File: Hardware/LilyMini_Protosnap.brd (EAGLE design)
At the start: 77.5 x 53.3 mm, 77 parts, among them Q1 ZXMP6A13F, U1 SAMD11D14A-M, U2 AP2112K-3.3V, U3 ALS-PT19, Y1 32.768kHz

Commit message: Minor tweaks per board review checklist
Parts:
- LOGO4: value (none) -> SFE_LOGO_NAME.1_INCH
- renumbered U$3 to LOGO4
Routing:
- net !RST!: track 26.5 -> 28.9 mm
- net !RST!1: track 18.7 -> 20.0 mm
- net GND: vias 12 -> 11
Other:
- board text added: "NOTE 31 MIL / 0.8MM BOARD THICKNESS"
- board text added: "ROUTE OUT"
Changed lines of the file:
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@@
 <layer number="14" name="Route14" color="1" fill="6" visible="no" active="no"/>
 <layer number="15" name="Route15" color="4" fill="6" visible="no" active="no"/>
-<layer number="16" name="Bottom" color="1" fill="1" visible="yes" active="yes"/>
-<layer number="17" name="Pads" color="2" fill="1" visible="yes" active="yes"/>
-<layer number="18" name="Vias" color="2" fill="1" visible="yes" active="yes"/>
-<layer number="19" name="Unrouted" color="6" fill="1" visible="yes" active="yes"/>
+<layer number="16" name="Bottom" color="1" fill="1" visible="no" active="yes"/>
+<layer number="17" name="Pads" color="2" fill="1" visible="no" active="yes"/>
+<layer number="18" name="Vias" color="2" fill="1" visible="no" active="yes"/>
+<layer number="19" name="Unrouted" color="6" fill="1" visible="no" active="yes"/>
 <layer number="20" name="Dimension" color="15" fill="1" visible="yes" active="yes"/>
 <layer number="21" name="tPlace" color="7" fill="1" visible="no" active="yes"/>
-<layer number="22" name="bPlace" color="7" fill="1" visible="yes" active="yes"/>
+<layer number="22" name="bPlace" color="7" fill="1" visible="no" active="yes"/>
 <layer number="23" name="tOrigins" color="15" fill="1" visible="no" active="yes"/>
-<layer number="24" name="bOrigins" color="15" fill="1" visible="yes" active="yes"/>
+<layer number="24" name="bOrigins" color="15" fill="1" visible="no" active="yes"/>
 <layer number="25" name="tNames" color="7" fill="1" visible="no" active="yes"/>
 <layer number="26" name="bNames" color="7" fill="1" visible="no" active="yes"/>
@@
 <layer number="28" name="bValues" color="7" fill="1" visible="no" active="yes"/>
 <layer number="29" name="tStop" color="7" fill="3" visible="no" active="yes"/>
-<layer number="30" name="bStop" color="7" fill="6" visible="yes" active="yes"/>
+<layer number="30" name="bStop" color="7" fill="6" visible="no" active="yes"/>
 <layer number="31" name="tCream" color="7" fill="4" visible="no" active="yes"/>
 <layer number="32" name="bCream" color="7" fill="5" visible="no" active="yes"/>
@@
 <layer number="37" name="tTest" color="7" fill="1" visible="no" active="yes"/>
 <layer number="38" name="bTest" color="7" fill="1" visible="no" active="yes"/>
-<layer number="39" name="tKeepout" color="4" fill="11" visible="yes" active="yes"/>
+<layer number="39" name="tKeepout" color="4" fill="11" visible="no" active="yes"/>
 <layer number="40" name="bKeepout" color="1" fill="11" visible="no" active="yes"/>
-<layer number="41" name="tRestrict" color="4" fill="10" visible="yes" active="yes"/>
+<layer number="41" name="tRestrict" color="4" fill="10" visible="no" active="yes"/>
 <layer number="42" name="bRestrict" color="1" fill="10" visible="no" active="yes"/>
 <layer number="43" name="vRestrict" color="2" fill="10" visible="no" active="yes"/>
@@
 <layer number="45" name="Holes" color="7" fill="1" visible="no" active="yes"/>
 <layer number="46" name="Milling" color="3" fill="1" visible="no" active="yes"/>
-<layer number="47" name="Measures" color="7" fill="1" visible="yes" active="yes"/>
+<layer number="47" name="Measures" color="7" fill="1" visible="no" active="yes"/>
 <layer number="48" name="Document" color="7" fill="1" visible="no" active="yes"/>
 <layer number="49" name="Reference" color="7" fill="1" visible="no" active="yes"/>
@@
 G 6
 B 7</text>
+<text x="38.735" y="-7.62" size="1.778" layer="51" align="center">NOTE 31 MIL / 0.8MM BOARD THICKNESS</text>
+<text x="39.52875" y="7.14375" size="0.6096" layer="20" ratio="10" align="center">ROUTE OUT</text>
+<text x="39.21125" y="43.65625" size="0.6096" layer="20" ratio="10" align="center">ROUTE OUT</text>
+<text x="67.78625" y="39.21125" size="0.6096" layer="20" ratio="10" align="center">ROUTE OUT</text>
+<text x="67.945" y="33.17875" size="0.6096" layer="20" ratio="10" align="center">ROUTE OUT</text>
+<text x="67.945" y="30.95625" size="0.6096" layer="20" ratio="10" align="center">ROUTE OUT</text>
+<text x="67.945" y="24.92375" size="0.6096" layer="20" ratio="10" align="center">ROUTE OUT</text>
+<text x="67.945" y="20.16125" size="0.6096" layer="20" ratio="10" align="center">ROUTE OUT</text>
+<text x="67.945" y="14.12875" size="0.6096" layer="20" ratio="10" align="center">ROUTE OUT</text>
+<text x="67.945" y="5.87375" size="0.6096" layer="20" ratio="10" align="center">ROUTE OUT</text>
+<text x="12.065" y="7.14375" size="0.6096" layer="20" ratio="10" align="center">ROUTE OUT</text>
+<text x="12.065" y="15.71625" size="0.6096" layer="20" ratio="10" align="center">ROUTE OUT</text>
+<text x="12.7" y="50.8" size="0.6096" layer="20" ratio="10" align="center">ROUTE OUT</text>
+<text x="23.495" y="34.29" size="0.6096" layer="20" ratio="10" rot="R60" align="center">ROUTE OUT</text>
+<text x="55.245" y="16.35125" size="0.6096" layer="20" ratio="10" rot="R60" align="center">ROUTE OUT</text>
+<text x="55.245" y="34.29" size="0.6096" layer="20" ratio="10" rot="R120" align="center">ROUTE OUT</text>
+<text x="23.65375" y="16.1925" size="0.6096" layer="20" ratio="10" rot="R120" align="center">ROUTE OUT</text>
+<text x="3.96875" y="35.40125" size="0.6096" layer="20" ratio="10" rot="R120" align="center">ROUTE OUT</text>
+<text x="21.59" y="35.71875" size="0.6096" layer="20" ratio="10" rot="R60" align="center">ROUTE OUT</text>
 </plain>
 <attributes>
@@
 <element name="JP24" library="LilyPad-Wearables" package="PETAL-SMALL-2SIDE" value="" x="63.5" y="36.195" rot="R270"/>
 <element name="JP26" library="LilyPad-Wearables" package="PETAL-SMALL-2SIDE" value="" x="63.5" y="27.94" rot="R270"/>
-<element name="U$3" library="SparkFun-Aesthetics" package="SFE_LOGO_NAME_.1" value="" x="45.72" y="44.92625" rot="MR0"/>
 <element name="U$4" library="SparkFun-Aesthetics" package="SFE_LOGO_FLAME_COPPER_EXPOSED_.1" value="" x="39.21125" y="47.625" rot="MR0"/>
 <element name="FD2" library="SparkFun-Aesthetics" package="MICRO-FIDUCIAL" value="FIDUCIALUFIDUCIAL" x="73.66" y="3.81"/>
@@
 <element name="FD3" library="SparkFun-Aesthetics" package="MICRO-FIDUCIAL" value="FIDUCIALUFIDUCIAL" x="3.81" y="49.53" rot="MR0"/>
 <element name="FD4" library="SparkFun-Aesthetics" package="MICRO-FIDUCIAL" value="FIDUCIALUFIDUCIAL" x="73.66" y="3.81" rot="MR0"/>
+<element name="LOGO4" library="SparkFun-Aesthetics" package="SFE_LOGO_NAME_.1" value="SFE_LOGO_NAME.1_INCH" x="45.72" y="44.92625" rot="MR0"/>
 </elements>
 <signals>
@@
 <contactref element="JP9" pad="P$1"/>
 <wire x1="30.7975" y1="23.1775" x2="38.1" y2="15.875" width="0.3048" layer="1"/>
-<wire x1="43.815" y1="15.875" x2="45.72" y2="15.875" width="0.3048" layer="16"/>
-<wire x1="45.72" y1="15.875" x2="47.205" y2="17.36" width="0.3048" layer="16"/>
+<wire x1="43.815" y1="15.875" x2="46.99" y2="15.875" width="0.3048" layer="16"/>
+<wire x1="46.99" y1="15.875" x2="48.475" y2="17.36" width="0.3048" layer="16"/>
 <contactref element="R5" pad="2"/>
-<wire x1="47.205" y1="17.36" x2="47.205" y2="18.415" width="0.3048" layer="16"/>
+<wire x1="48.475" y1="17.36" x2="48.475" y2="18.2" width="0.3048" layer="16"/>
+<wire x1="48.475" y1="18.2" x2="48.26" y2="18.415" width="0.3048" layer="16"/>
+<wire x1="48.26" y1="18.415" x2="47.205" y2="18.415" width="0.3048" layer="16"/>
 </signal>
 <signal name="USB5V">
@@
 <via x="45.085" y="17.145" extent="1-16" drill="0.508"/>
 <via x="51.435" y="21.59" extent="1-16" drill="0.508"/>
-<via x="48.26" y="15.875" extent="1-16" drill="0.508"/>
 <contactref element="S2" pad="4"/>
 <contactref element="S2" pad="3"/>
@@
 <wire x1="35.2425" y1="23.1775" x2="38.735" y2="19.685" width="0.3048" layer="1"/>
 <wire x1="38.735" y1="19.685" x2="43.815" y2="19.685" width="0.3048" layer="1"/>
-<wire x1="45.505" y1="18.415" x2="45.505" y2="19.685" width="0.3048" layer="16"/>
 <wire x1="45.505" y1="19.685" x2="43.815" y2="19.685" width="0.3048" layer="16"/>
 <via x="43.815" y="19.685" extent="1-16" drill="0.508"/>
+<wire x1="45.505" y1="18.415" x2="44.45" y2="18.415" width="0.3048" layer="16"/>
+<wire x1="44.45" y1="18.415" x2="43.815" y2="19.05" width="0.3048" layer="16"/>
+<wire x1="43.815" y1="19.05" x2="43.815" y2="19.685" width="0.3048" layer="16"/>
 </signal>
 <signal name="X2">

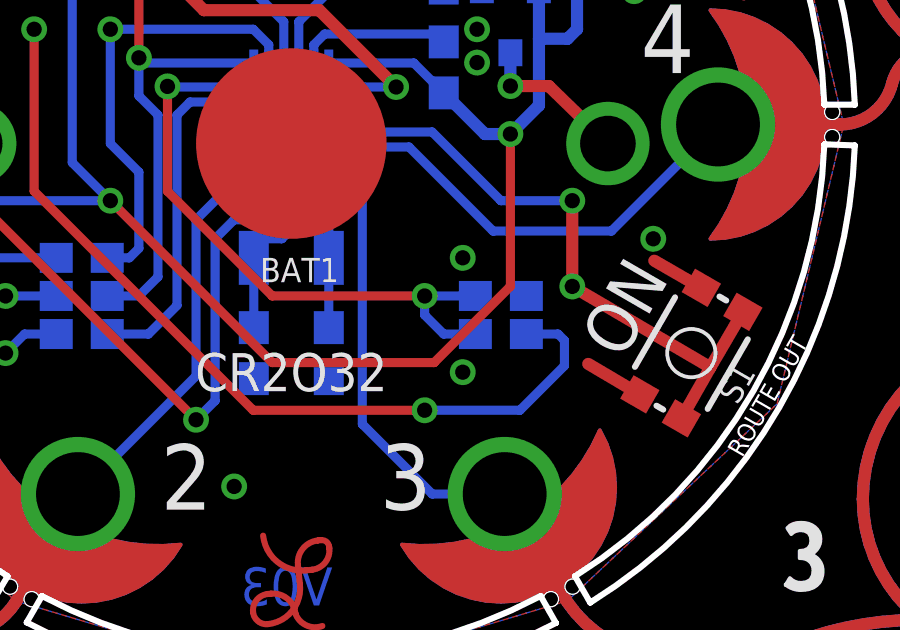
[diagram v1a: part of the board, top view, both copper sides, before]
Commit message: Minor changes based on AC and Bob's advice
Reduced paste on QFN and USB footprints by 25%
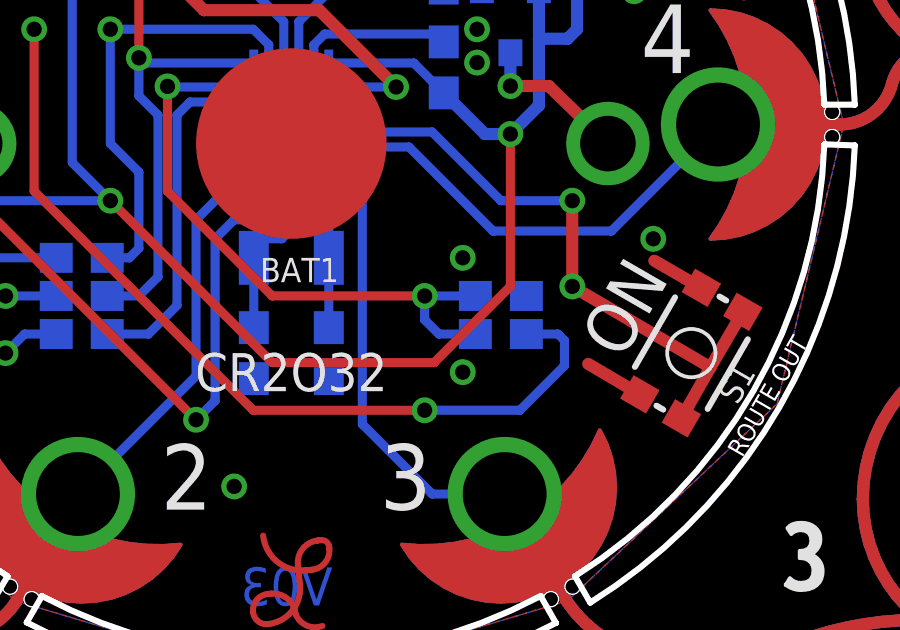
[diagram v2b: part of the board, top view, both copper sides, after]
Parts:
- JP1: value (none) -> USB_MICROB_PLUGUSB-B-MICRO-SMD-VERT
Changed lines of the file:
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@@
 <grid distance="0.025" unitdist="inch" unit="inch" style="lines" multiple="4" display="yes" altdistance="0.00625" altunitdist="inch" altunit="inch"/>
 <layers>
-<layer number="1" name="Top" color="4" fill="1" visible="no" active="yes"/>
+<layer number="1" name="Top" color="4" fill="1" visible="yes" active="yes"/>
 <layer number="2" name="Route2" color="1" fill="3" visible="no" active="no"/>
 <layer number="3" name="Route3" color="4" fill="3" visible="no" active="no"/>
@@
 <layer number="15" name="Route15" color="4" fill="6" visible="no" active="no"/>
 <layer number="16" name="Bottom" color="1" fill="1" visible="no" active="yes"/>
-<layer number="17" name="Pads" color="2" fill="1" visible="no" active="yes"/>
-<layer number="18" name="Vias" color="2" fill="1" visible="no" active="yes"/>
+<layer number="17" name="Pads" color="2" fill="1" visible="yes" active="yes"/>
+<layer number="18" name="Vias" color="2" fill="1" visible="yes" active="yes"/>
 <layer number="19" name="Unrouted" color="6" fill="1" visible="no" active="yes"/>
 <layer number="20" name="Dimension" color="15" fill="1" visible="yes" active="yes"/>
-<layer number="21" name="tPlace" color="7" fill="1" visible="no" active="yes"/>
+<layer number="21" name="tPlace" color="7" fill="1" visible="yes" active="yes"/>
 <layer number="22" name="bPlace" color="7" fill="1" visible="no" active="yes"/>
 <layer number="23" name="tOrigins" color="15" fill="1" visible="no" active="yes"/>
@@
 <layer number="27" name="tValues" color="7" fill="1" visible="no" active="yes"/>
 <layer number="28" name="bValues" color="7" fill="1" visible="no" active="yes"/>
-<layer number="29" name="tStop" color="7" fill="3" visible="no" active="yes"/>
+<layer number="29" name="tStop" color="7" fill="3" visible="yes" active="yes"/>
 <layer number="30" name="bStop" color="7" fill="6" visible="no" active="yes"/>
-<layer number="31" name="tCream" color="7" fill="4" visible="no" active="yes"/>
+<layer number="31" name="tCream" color="7" fill="4" visible="yes" active="yes"/>
 <layer number="32" name="bCream" color="7" fill="5" visible="no" active="yes"/>
 <layer number="33" name="tFinish" color="6" fill="3" visible="no" active="yes"/>
@@
 <layer number="37" name="tTest" color="7" fill="1" visible="no" active="yes"/>
 <layer number="38" name="bTest" color="7" fill="1" visible="no" active="yes"/>
-<layer number="39" name="tKeepout" color="4" fill="11" visible="no" active="yes"/>
+<layer number="39" name="tKeepout" color="4" fill="11" visible="yes" active="yes"/>
 <layer number="40" name="bKeepout" color="1" fill="11" visible="no" active="yes"/>
-<layer number="41" name="tRestrict" color="4" fill="10" visible="no" active="yes"/>
+<layer number="41" name="tRestrict" color="4" fill="10" visible="yes" active="yes"/>
 <layer number="42" name="bRestrict" color="1" fill="10" visible="no" active="yes"/>
 <layer number="43" name="vRestrict" color="2" fill="10" visible="no" active="yes"/>
@@
 <layer number="45" name="Holes" color="7" fill="1" visible="no" active="yes"/>
 <layer number="46" name="Milling" color="3" fill="1" visible="no" active="yes"/>
-<layer number="47" name="Measures" color="7" fill="1" visible="no" active="yes"/>
+<layer number="47" name="Measures" color="7" fill="1" visible="yes" active="yes"/>
 <layer number="48" name="Document" color="7" fill="1" visible="no" active="yes"/>
 <layer number="49" name="Reference" color="7" fill="1" visible="no" active="yes"/>
 <layer number="50" name="dxf" color="7" fill="1" visible="no" active="no"/>
-<layer number="51" name="tDocu" color="7" fill="1" visible="no" active="yes"/>
+<layer number="51" name="tDocu" color="7" fill="1" visible="yes" active="yes"/>
 <layer number="52" name="bDocu" color="7" fill="1" visible="no" active="yes"/>
 <layer number="53" name="tGND_GNDA" color="7" fill="9" visible="no" active="no"/>
@@
 <elements>
 <element name="FRAME1" library="SparkFun-Aesthetics" package="CREATIVE_COMMONS" value="FRAME-LETTER" x="4.445" y="-17.78"/>
-<element name="JP1" library="mike-temp" package="USB-B-MICRO-SMD_VERT" value="" x="39.37" y="38.4175" smashed="yes">
+<element name="JP1" library="mike-temp" package="USB-B-MICRO-SMD_VERT" value="USB_MICROB_PLUGUSB-B-MICRO-SMD-VERT" x="39.37" y="38.4175" smashed="yes">
 <attribute name="NAME" x="40.275" y="40.4975" size="0.8128" layer="25" align="bottom-right"/>
 <attribute name="VALUE" x="40.37" y="35.4175" size="0.4064" layer="27"/>
@@
 <wire x1="45.505" y1="19.685" x2="43.815" y2="19.685" width="0.3048" layer="16"/>
 <via x="43.815" y="19.685" extent="1-16" drill="0.508"/>
-<wire x1="45.505" y1="18.415" x2="44.45" y2="18.415" width="0.3048" layer="16"/>
-<wire x1="44.45" y1="18.415" x2="43.815" y2="19.05" width="0.3048" layer="16"/>
-<wire x1="43.815" y1="19.05" x2="43.815" y2="19.685" width="0.3048" layer="16"/>
+<wire x1="45.505" y1="18.415" x2="44.29125" y2="18.415" width="0.3048" layer="16"/>
+<wire x1="44.29125" y1="18.415" x2="43.815" y2="18.89125" width="0.3048" layer="16"/>
+<wire x1="43.815" y1="18.89125" x2="43.815" y2="19.685" width="0.3048" layer="16"/>
 </signal>
 <signal name="X2">
